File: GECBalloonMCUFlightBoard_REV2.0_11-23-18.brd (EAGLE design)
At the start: 160 x 100 mm, 68 parts, among them IC1 PIC32MX360F512L, U1 ADS1118, U2 ADS1118, X2 MALE_VGA, Y1 SG-636PCW_50.0000MC3__ROHS

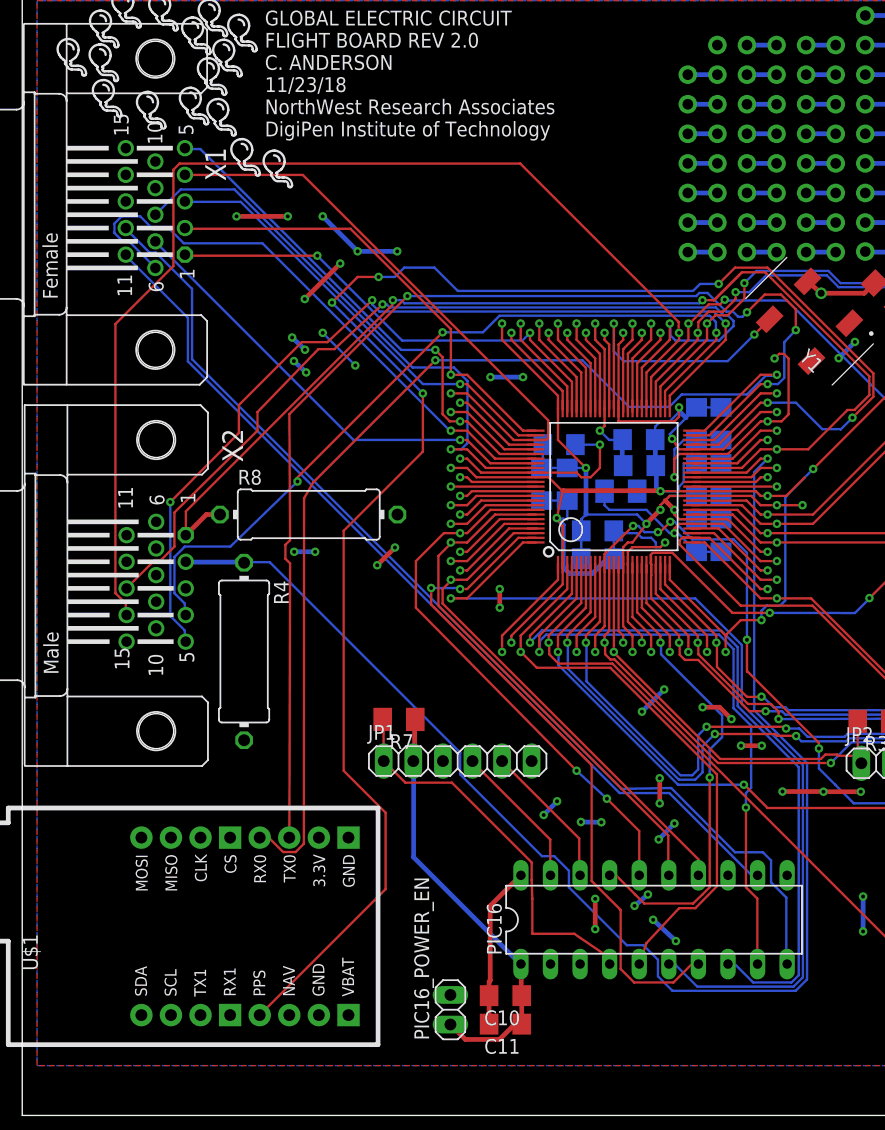
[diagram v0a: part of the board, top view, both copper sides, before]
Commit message: Added PIC16_XBEE_SLEEP pin to the VGA connector X1 on PIN14
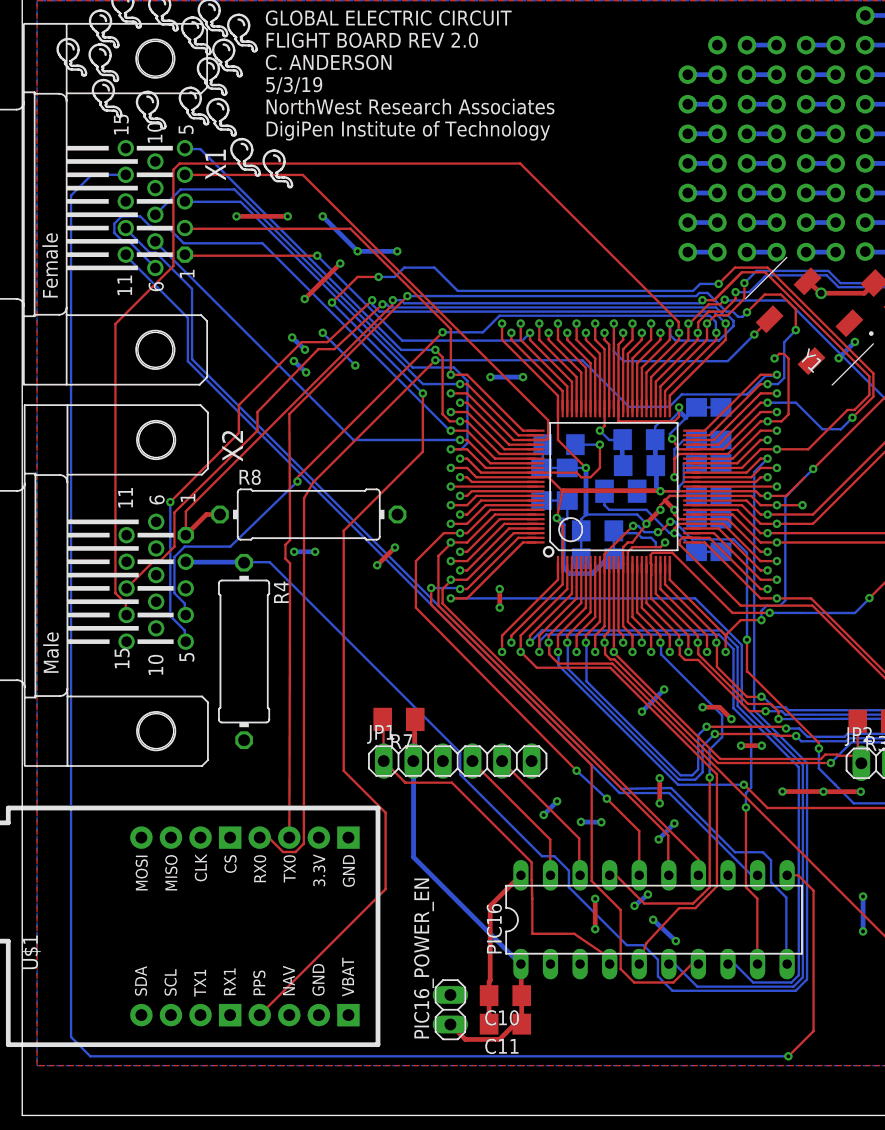
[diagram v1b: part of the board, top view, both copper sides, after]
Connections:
- removed net N$20: PIC16.11
- new net PIC16_XBEE_SLEEP: PIC16.11, X1.14
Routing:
- net PIC16_XBEE_SLEEP: track 0.00 -> 157.9 mm, vias 0 -> 1
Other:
- board text added: "GLOBAL ELECTRIC CIRCUIT FLIGHT BOARD REV 2.0 C. ANDERSON 5/3/19 NorthWest Research Associates DigiPen Institute of Technology"
- board text removed: "GLOBAL ELECTRIC CIRCUIT FLIGHT BOARD REV 2.0 C. ANDERSON 11/23/18 NorthWest Research Associates DigiPen Institute of Technology"
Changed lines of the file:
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@@
 FLIGHT BOARD REV 2.0
 C. ANDERSON
-11/23/18
+5/3/19
 NorthWest Research Associates
 DigiPen Institute of Technology</text>
@@
 <wire x1="8.89" y1="73.8252" x2="8.89" y2="73.913" width="0.2032" layer="16"/>
 </signal>
-<signal name="N$20">
-<contactref element="PIC16" pad="11"/>
-</signal>
 <signal name="PIC16_3V3" class="1">
 <contactref element="PIC16" pad="1"/>
@@
 <wire x1="70.272" y1="58.928" x2="70.286" y2="58.914" width="0.2032" layer="16"/>
 </signal>
+<signal name="PIC16_XBEE_SLEEP">
+<contactref element="X1" pad="14"/>
+<contactref element="PIC16" pad="11"/>
+<wire x1="65.68" y1="20.62" x2="66.629" y2="20.62" width="0.2032" layer="1"/>
+<wire x1="66.629" y1="20.62" x2="67.945" y2="19.304" width="0.2032" layer="1"/>
+<wire x1="67.945" y1="19.304" x2="67.945" y2="7.239" width="0.2032" layer="1"/>
+<wire x1="67.945" y1="7.239" x2="65.786" y2="5.08" width="0.2032" layer="1"/>
+<via x="65.786" y="5.08" extent="1-16" drill="0.3302"/>
+<wire x1="65.786" y1="5.08" x2="5.842" y2="5.08" width="0.2032" layer="16"/>
+<wire x1="5.842" y1="5.08" x2="4.191" y2="6.731" width="0.2032" layer="16"/>
+<wire x1="4.191" y1="6.731" x2="4.191" y2="78.994" width="0.2032" layer="16"/>
+<wire x1="4.191" y1="78.994" x2="5.969" y2="80.772" width="0.2032" layer="16"/>
+<wire x1="5.969" y1="80.772" x2="8.889" y2="80.772" width="0.2032" layer="16"/>
+<wire x1="8.889" y1="80.772" x2="8.89" y2="80.771" width="0.2032" layer="16"/>
+</signal>
 </signals>

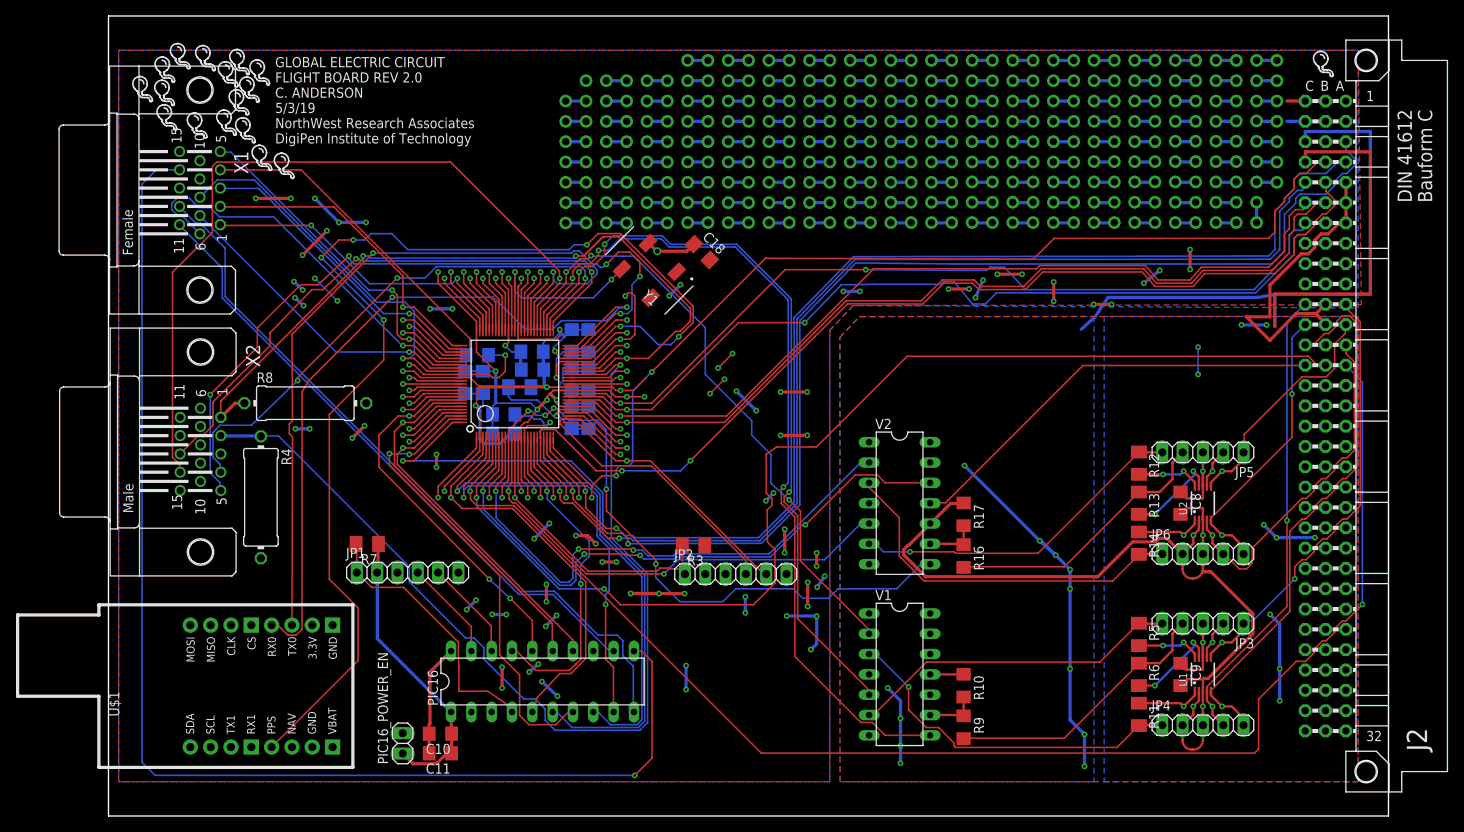
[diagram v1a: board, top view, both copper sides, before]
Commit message: Added GPS power mosfet and GPS standby mosfet.
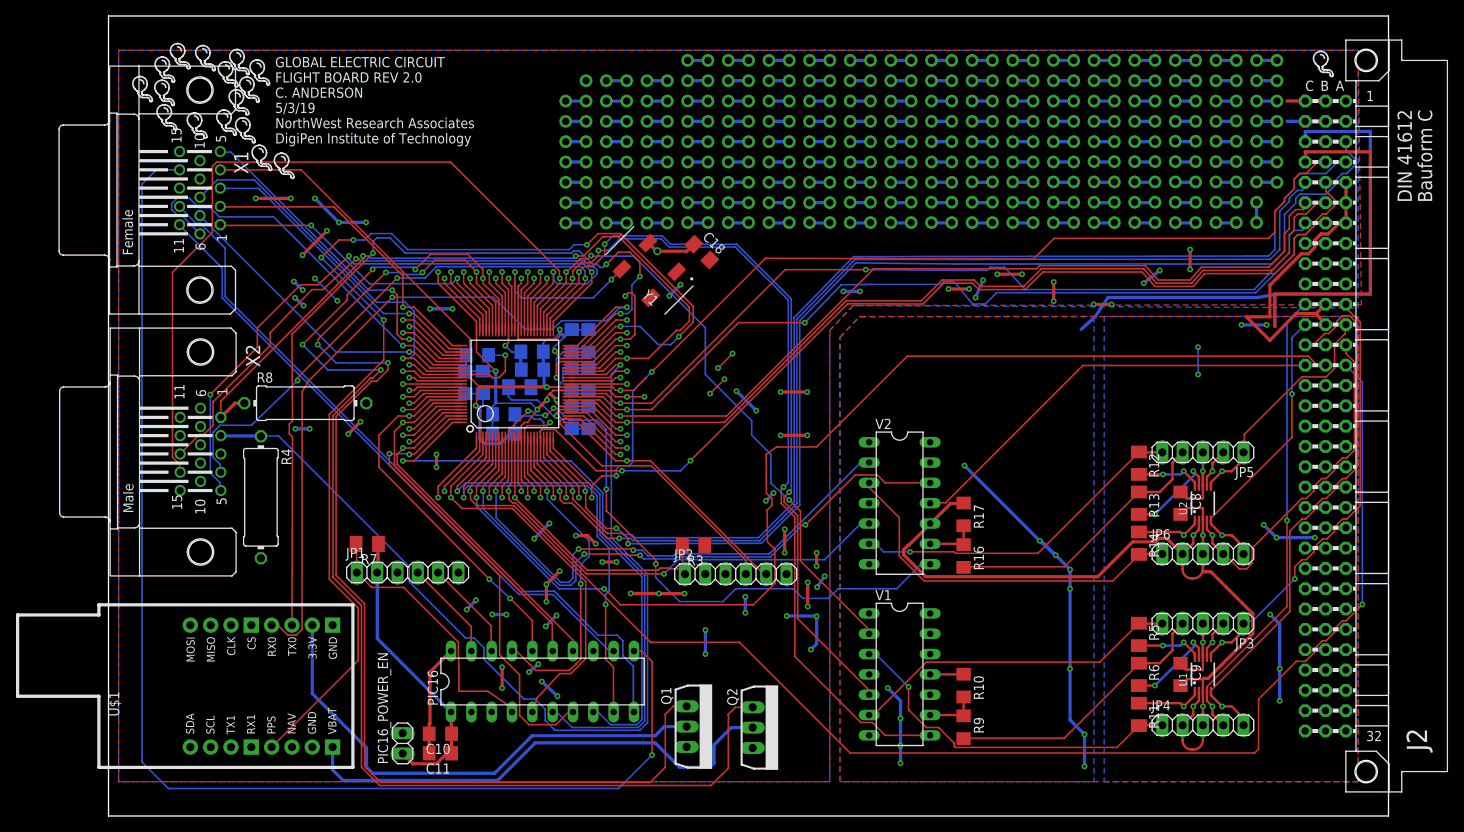
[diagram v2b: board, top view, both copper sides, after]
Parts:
- added Q1, Q2: IRF3704L-V, transistor-power:TO262-V
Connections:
- new net GPS_3V3_OUT: Q1.2, U$1.2
- new net GPS_3V3_SGNL: IC1.69, Q1.1
- new net GPS_VBAT_OUT: Q2.2, U$1.16
- new net GPS_VBAT_SGNL: IC1.68, Q2.1
- new net N$20: IC1.19
- net +3V3: now also Q1.3, Q2.3; no longer U$1.2
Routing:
- net GPS_VBAT_SGNL: track 0.00 -> 160.0 mm, vias 0 -> 5
- net GPS_3V3_SGNL: track 0.00 -> 147.5 mm, vias 0 -> 5
- net GPS_3V3_OUT: track 0.00 -> 63.3 mm
- net GPS_VBAT_OUT: track 0.00 -> 62.5 mm
- net N$70: track 8.59 -> 0.00 mm, vias 1 -> 0
- net N$95: track 8.59 -> 0.00 mm, vias 1 -> 0
- net N$20: track 0.00 -> 8.59 mm, vias 0 -> 1
- net N$69: track 7.63 -> 0.00 mm, vias 1 -> 0
- net RB_TEMP: track 99.7 -> 96.3 mm
- net U2RX: track 102.9 -> 105.3 mm
- net GND_3V3: track 201.8 -> 204.2 mm, vias 57 -> 58
- net PIC16_XBEE_SLEEP: track 157.9 -> 159.1 mm
- net PBUS0: vias 2 -> 3

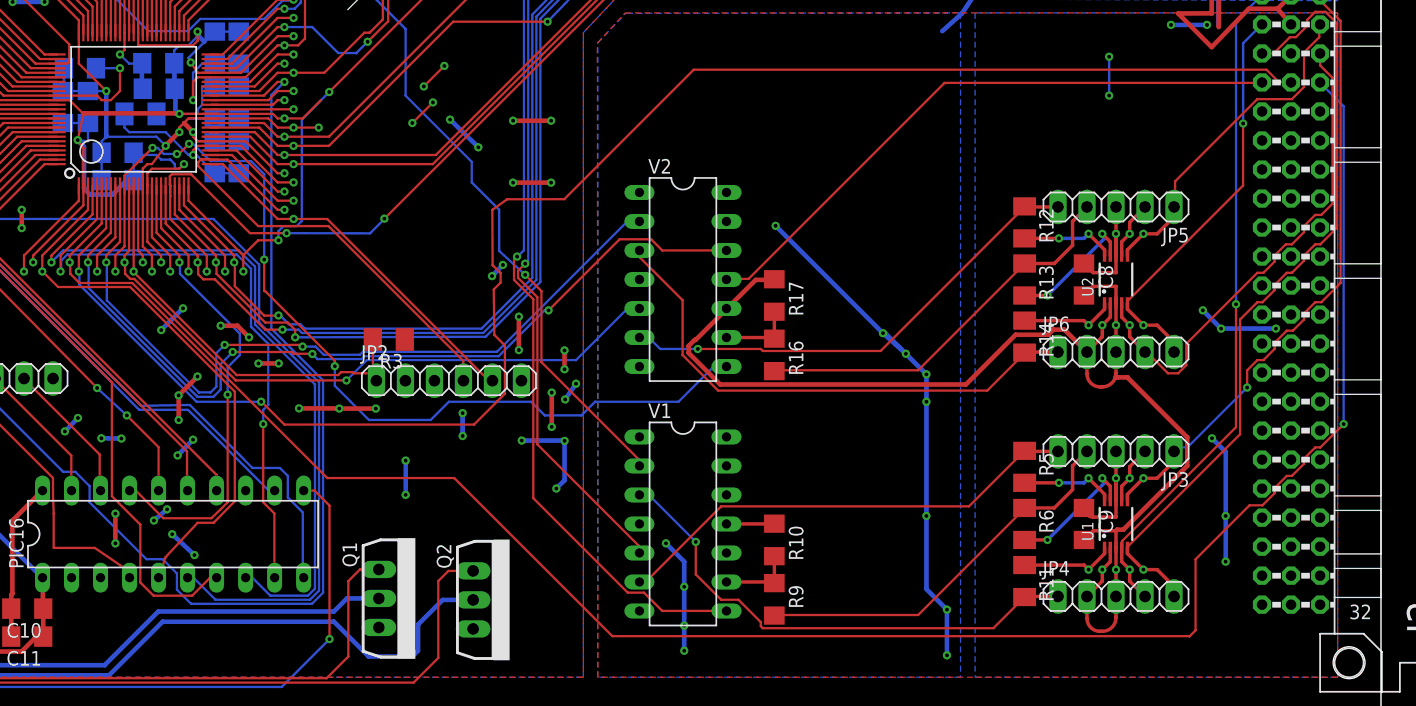
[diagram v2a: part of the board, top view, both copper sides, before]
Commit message: So far, manage to rip up old traces without totally losing the PIC32's fan out
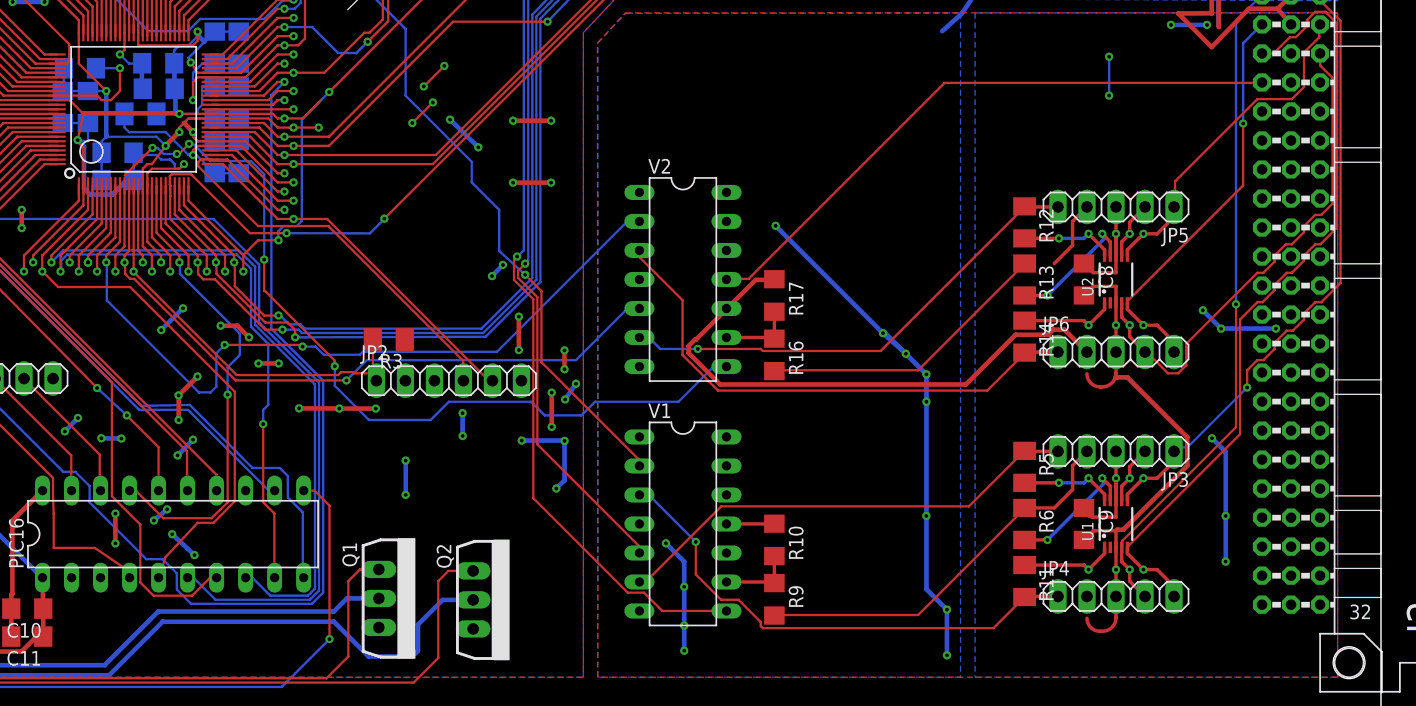
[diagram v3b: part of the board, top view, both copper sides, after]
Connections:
- removed net ADC2_DIN: JP5.5, R12.1, V2.6
- removed net ADC2_SCK: JP6.1, R14.2, V2.3
- removed net PIC_COND_EN: IC1.8, V2.12
- removed net SCK2: IC1.10, V2.2
- removed net SDO2: IC1.12, V2.5
- new net N$67: U1.2
- new net N$69: JP4.2
- new net N$70: U2.2
- new net N$79: JP6.2
- new net N/A1: IC1.6
- new net N/A2: IC1.7
- new net N/A3: IC1.8
- new net PIC_CHARGE_PROBE_0: IC1.10
- new net PIC_CHARGE_PROBE_1: IC1.11
- new net PIC_COND_EN_NEW2: IC1.12
- net ADC1_DIN: now also JP5.5, R12.1, V2.6
- net ADC1_DOUT: now also R13.1
- net ADC1_SCK: now also JP6.1, R14.2, V2.3
- net ADC2_DOUT: no longer R13.1
- net CHARGE_PROBE_0: no longer IC1.6
- net CHARGE_PROBE_1: no longer IC1.7
- net GND_5V: no longer JP4.2, JP6.2, U1.2, U2.2
- net SDI2: no longer IC1.11
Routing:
- net CHARGE_PROBE_0: track 176.1 -> 0.00 mm, vias 2 -> 0
- net CHARGE_PROBE_1: track 145.6 -> 0.00 mm, vias 2 -> 0
- net PIC_COND_EN: track 77.5 -> 0.00 mm, vias 4 -> 0
- net SCK2: track 69.2 -> 0.00 mm, vias 3 -> 0
- net PIC_CHARGE_PROBE_0: track 0.00 -> 69.1 mm, vias 0 -> 3
- net SDO2: track 59.4 -> 0.00 mm, vias 2 -> 0
- net PIC_COND_EN_NEW2: track 0.00 -> 59.3 mm, vias 0 -> 2
- net ADC2_SCK: track 46.3 -> 0.00 mm
- net ADC1_SCK: track 44.5 -> 90.8 mm
- net ADC2_DIN: track 42.4 -> 0.00 mm, vias 1 -> 0
- net ADC1_DIN: track 41.4 -> 83.8 mm, vias 0 -> 1
- net GND_5V: track 188.0 -> 173.8 mm, vias 4 -> 2
- net SDI2: track 83.3 -> 74.5 mm, vias 6 -> 5
- net N/A2: track 0.00 -> 8.49 mm, vias 0 -> 1
- net N/A1: track 0.00 -> 7.86 mm, vias 0 -> 1
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
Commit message: Part way done
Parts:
- added R1, R18: 680, resistor:R1206
- added R15, R19: 510, resistor:R1206
- R16: value 510 -> 680
- R17: value 680 -> 510
- moved R16 24.1 mm to (94.7, 53.3), flipped to the bottom, turned to 90 degrees
- moved R17 16.8 mm to (100.7, 53.3), flipped to the bottom, turned to 90 degrees
- moved R10 5.63 mm to (110.9, 12.4), flipped to the bottom, turned to 0 degrees
- flipped R9 to the bottom
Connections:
- removed net ADC2_DIVIDED: R16.1, R17.2, V2.9
- removed net ADC2_DOUT: JP5.4, R16.2
- removed net N$67: U1.2
- removed net N$69: JP4.2
- removed net N$70: U2.2
- removed net N$79: JP6.2
- removed net PIC_COND_EN_NEW2: IC1.12
- removed net SDI2: V2.8
- new net !SS1_5V: JP4.2, U1.2, V2.8
- new net !SS2_5V: JP6.2, U2.2, V2.11
- new net CHRG_PRB_0_5V: R17.1, V2.3
- new net CHRG_PRB_1_5V: R19.1, V2.6
- new net COND_EN_5V: R15.1, V1.11
- new net PIC_COND_EN: IC1.12, V1.12
- net !SS1: now also V2.9
- net !SS2: now also V2.12
- net ADC1_DIN: no longer V2.6
- net ADC1_DOUT: now also JP5.4
- net ADC1_SCK: no longer V2.3
- net CHARGE_PROBE_0: now also R16.2, R17.2
- net CHARGE_PROBE_1: now also R18.2, R19.2
- net CONDUCTIVITY_ENABLE: now also R1.2, R15.2; no longer V2.11
- net GND_5V: now also R1.1, R16.1, R18.1; no longer R17.1, V1.11, V1.12
- net PIC_CHARGE_PROBE_0: now also V2.2
- net PIC_CHARGE_PROBE_1: now also V2.5
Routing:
- net CHARGE_PROBE_0: track 0.00 -> 77.4 mm, vias 0 -> 1
- net SDI2: track 74.5 -> 0.00 mm, vias 5 -> 0
- net !SS1: track 0.00 -> 65.2 mm, vias 0 -> 4
- net PIC_COND_EN_NEW2: track 59.3 -> 0.00 mm, vias 2 -> 0
- net PIC_COND_EN: track 0.00 -> 59.3 mm, vias 0 -> 2
- net CHARGE_PROBE_1: track 0.00 -> 59.2 mm, vias 0 -> 1
- net GND_5V: track 173.8 -> 128.5 mm, vias 2 -> 3
- net ADC1_DIN: track 83.8 -> 44.4 mm, vias 1 -> 0
- net ADC1_SCK: track 90.8 -> 52.2 mm
- net CHRG_PRB_1_5V: track 0.00 -> 32.1 mm, vias 0 -> 1
- net ADC2_DOUT: track 31.8 -> 0.00 mm
- net ADC1_DOUT: track 34.6 -> 49.8 mm, vias 0 -> 2
- net CHRG_PRB_0_5V: track 0.00 -> 13.2 mm
- net CONDUCTIVITY_ENABLE: track 54.0 -> 64.6 mm
- net N$97: track 9.26 -> 0.00 mm, vias 1 -> 0
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
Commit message: Routed a lot of signals, fixed a lot of errors and nearly lost my mind. Everything on my checklist is complete now, though.
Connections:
- net N$20 renamed RE9
- net N/A1 renamed RC1
- net N/A2 renamed RC2
- net N/A3 renamed RC3
- new net RC4: IC1.9
- new net RG15: IC1.1
- new net TMS: IC1.17
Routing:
- net !SS2: track 0.00 -> 116.1 mm, vias 0 -> 7
- net PIC_CHARGE_PROBE_1: track 7.83 -> 68.9 mm, vias 1 -> 5
- net !SS1_5V: track 0.00 -> 58.7 mm, vias 0 -> 2
- net !SS2_5V: track 0.00 -> 45.2 mm, vias 0 -> 3
- net +5V: track 146.4 -> 172.5 mm, vias 24 -> 32
- net ADC1_DIN: track 44.4 -> 68.0 mm, vias 0 -> 1
- net ADC1_SCK: track 52.2 -> 72.9 mm, vias 1 -> 3
- net GND_5V: track 128.5 -> 148.0 mm, vias 3 -> 9
- net PIC_COND_EN: track 59.3 -> 73.0 mm
- net CONDUCTIVITY_ENABLE: track 64.6 -> 78.1 mm, vias 0 -> 1
- net ADC1_DOUT: track 49.8 -> 62.4 mm, vias 2 -> 3
- net +3V3: track 179.5 -> 190.3 mm, vias 53 -> 62
- net RG15: track 0.00 -> 9.59 mm, vias 0 -> 1
- net N$86: track 9.59 -> 0.00 mm, vias 1 -> 0
- net N$87: track 8.62 -> 0.00 mm, vias 1 -> 0
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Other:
- board text added: "+3V3"
- board text added: "+5V"
- board text added: "GND_3V3"
- board text added: "GND_5V"
